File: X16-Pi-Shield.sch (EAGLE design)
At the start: 55 parts, among them J1 CONN_DF13-4P-1.25DSA, J2 CONN_DF13-4P-1.25DSA, J3 CONN_DF13-4P-1.25DSA, Q2 2.5A/30V/105mΩ, Q3 220mA/50V/3.5Ω, Q4 220mA/50V/3.5Ω, Q5 220mA/50V/3.5Ω, U2 MAX1136EUA-T, Y2 ECS-80-S-4X

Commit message: edited schematic for new connector
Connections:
- net GPIO_6 renamed SA0
- removed net N$42: U$1.3V3@1
- new net CTRL: U$1.GPIO22
- new net DGND: U$1.GPIO6
- new net SA1: U$1.GPIO18
- new net SALERT: U$1.GPIO13
- net 3V3: now also U$1.3V3@1
- net GPIO_10: no longer U$1.GPIO6
- net GPIO_11: no longer U$1.GPIO22
- net GPIO_7: no longer U$1.GPIO18
- net GPIO_8: no longer U$1.GPIO12
- net GPIO_9: no longer U$1.GPIO13
- net SCL: now also U$1.GPIO12
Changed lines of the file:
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@@
 <attribute name="SPICEPREFIX" value="X"/>
 </part>
+<part name="FRAME3" library="SparkFun-Aesthetics" library_urn="urn:adsk.eagle:library:507" deviceset="FRAME-A4L" device=""/>
 </parts>
 <sheets>
@@
 </segment>
 </net>
-<net name="GPIO_7" class="0">
-<segment>
-<pinref part="U$1" gate="G$1" pin="GPIO18"/>
-<wire x1="139.7" y1="160.02" x2="139.7" y2="167.64" width="0.1524" layer="91"/>
-<label x="139.7" y="162.56" size="1.778" layer="95" rot="R90"/>
-</segment>
-</net>
 <net name="GPIO_2" class="0">
 <segment>
@@
 </segment>
 </net>
-<net name="GPIO_8" class="0">
-<segment>
-<pinref part="U$1" gate="G$1" pin="GPIO12"/>
-<wire x1="190.5" y1="160.02" x2="190.5" y2="167.64" width="0.1524" layer="91"/>
-<label x="190.5" y="162.56" size="1.778" layer="95" rot="R90"/>
-</segment>
-</net>
 <net name="GPIO_1" class="0">
 <segment>
@@
 </segment>
 </net>
-<net name="GPIO_6" class="0">
-<segment>
-<pinref part="U$1" gate="G$1" pin="GPIO21"/>
-<wire x1="210.82" y1="160.02" x2="210.82" y2="167.64" width="0.1524" layer="91"/>
-<label x="210.82" y="162.56" size="1.778" layer="95" rot="R90"/>
-</segment>
-</net>
 <net name="INT" class="0">
 <segment>
@@
 </segment>
 </net>
-<net name="GPIO_9" class="0">
-<segment>
-<pinref part="U$1" gate="G$1" pin="GPIO13"/>
-<wire x1="195.58" y1="132.08" x2="195.58" y2="127" width="0.1524" layer="91"/>
-<label x="195.58" y="121.92" size="1.778" layer="95" rot="R90"/>
-</segment>
-</net>
-<net name="GPIO_10" class="0">
-<segment>
-<pinref part="U$1" gate="G$1" pin="GPIO6"/>
-<wire x1="190.5" y1="132.08" x2="190.5" y2="127" width="0.1524" layer="91"/>
-<label x="190.5" y="121.92" size="1.778" layer="95" rot="R90"/>
-</segment>
-</net>
 <net name="RX1_INT" class="0">
 <segment>
@@
 </segment>
 </net>
-<net name="GPIO_11" class="0">
-<segment>
-<pinref part="U$1" gate="G$1" pin="GPIO22"/>
-<wire x1="149.86" y1="132.08" x2="149.86" y2="127" width="0.1524" layer="91"/>
-<label x="149.86" y="121.92" size="1.778" layer="95" rot="R90"/>
-</segment>
-</net>
 <net name="IMU_INT" class="0">
 <segment>
@@
 <wire x1="142.24" y1="45.72" x2="134.62" y2="45.72" width="0.1524" layer="91"/>
 <label x="137.16" y="45.72" size="1.778" layer="95"/>
-</segment>
-</net>
-<net name="N$42" class="0">
-<segment>
-<pinref part="U$1" gate="G$1" pin="3V3@1"/>
-<wire x1="114.3" y1="132.08" x2="114.3" y2="129.54" width="0.1524" layer="91"/>
 </segment>
 </net>
@@
 <wire x1="83.82" y1="170.18" x2="73.66" y2="170.18" width="0.1524" layer="91"/>
 </segment>
+<segment>
+<pinref part="U$1" gate="G$1" pin="3V3@1"/>
+<wire x1="114.3" y1="132.08" x2="114.3" y2="129.54" width="0.1524" layer="91"/>
+<label x="114.3" y="127" size="1.778" layer="95" rot="R90"/>
+</segment>
 </net>
 <net name="SCL" class="0">
@@
 <wire x1="45.72" y1="101.6" x2="33.02" y2="101.6" width="0.1524" layer="91"/>
 <label x="35.56" y="101.6" size="1.778" layer="95"/>
+</segment>
+<segment>
+<pinref part="U$1" gate="G$1" pin="GPIO12"/>
+<wire x1="190.5" y1="160.02" x2="190.5" y2="167.64" width="0.1524" layer="91"/>
+<label x="190.5" y="162.56" size="1.778" layer="95" rot="R90"/>
 </segment>
 </net>
@@
 </segment>
 </net>
+<net name="CTRL" class="0">
+<segment>
+<pinref part="U$1" gate="G$1" pin="GPIO22"/>
+<wire x1="149.86" y1="132.08" x2="149.86" y2="127" width="0.1524" layer="91"/>
+<label x="149.86" y="127" size="1.778" layer="95" rot="R90"/>
+</segment>
+</net>
+<net name="DGND" class="0">
+<segment>
+<pinref part="U$1" gate="G$1" pin="GPIO6"/>
+<wire x1="190.5" y1="132.08" x2="190.5" y2="127" width="0.1524" layer="91"/>
+<label x="190.5" y="124.46" size="1.778" layer="95" rot="R90"/>
+</segment>
+</net>
+<net name="SALERT" class="0">
+<segment>
+<pinref part="U$1" gate="G$1" pin="GPIO13"/>
+<wire x1="195.58" y1="132.08" x2="195.58" y2="127" width="0.1524" layer="91"/>
+<label x="195.58" y="121.92" size="1.778" layer="95" rot="R90"/>
+</segment>
+</net>
+<net name="SA1" class="0">
+<segment>
+<pinref part="U$1" gate="G$1" pin="GPIO18"/>
+<wire x1="139.7" y1="160.02" x2="139.7" y2="167.64" width="0.1524" layer="91"/>
+<label x="139.7" y="162.56" size="1.778" layer="95" rot="R90"/>
+</segment>
+</net>
+<net name="SA0" class="0">
+<segment>
+<pinref part="U$1" gate="G$1" pin="GPIO21"/>
+<wire x1="210.82" y1="160.02" x2="210.82" y2="167.64" width="0.1524" layer="91"/>
+<label x="210.82" y="162.56" size="1.778" layer="95" rot="R90"/>
+</segment>
+</net>
 </nets>
 </sheet>
@@
 </nets>
 </sheet>
+<sheet>
+<plain>
+</plain>
+<instances>
+<instance part="FRAME3" gate="G$1" x="0" y="0" smashed="yes">
+<attribute name="DRAWING_NAME" x="181.61" y="11.43" size="2.54" layer="94" font="vector"/>
+<attribute name="LAST_DATE_TIME" x="181.61" y="6.35" size="2.286" layer="94" font="vector"/>
+<attribute name="SHEET" x="195.58" y="1.27" size="2.54" layer="94" font="vector"/>
+<attribute name="DESIGNER" x="226.26" y="6.35" size="2.54" layer="94" font="vector"/>
+</instance>
+</instances>
+<busses>
+</busses>
+<nets>
+</nets>
+</sheet>
 </sheets>
 </schematic>
@@
 which will not be processed correctly with this version.
 </note>
+<note version="8.2" severity="warning">
+Since Version 8.2, EAGLE supports online libraries. The ids
+of those online libraries will not be understood (or retained)
+with this version.
+</note>
+<note version="8.3" severity="warning">
+Since Version 8.3, EAGLE supports URNs for individual library
+assets (packages, symbols, and devices). The URNs of those assets
+will not be understood (or retained) with this version.
+</note>
 </compatibility>

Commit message: added connector
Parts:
- added J4: SAMTEC-HTST-110-04-X-D-RAJ, SAMTEC-HTST-110-04-X-D-RA:SAMTEC-HTST-110-04-X-D-RAJ
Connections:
- net 5V: now also J4.1
- net CLK: now also J4.18
- net CS: now also J4.20
- net CTRL: now also J4.7
- net DGND: now also J4.9
- net GND: now also J4.3
- net GPIO1: now also J4.2
- net GPIO2: now also J4.4
- net GPIO3: now also J4.6
- net GPIO4: now also J4.8
- net MISO: now also J4.14
- net MOSI: now also J4.16
- net SA0: now also J4.19
- net SA1: now also J4.17
- net SALERT: now also J4.13
- net SCL: now also J4.15
- net SDA: now also J4.11
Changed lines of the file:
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@@
 </part>
 <part name="FRAME3" library="SparkFun-Aesthetics" library_urn="urn:adsk.eagle:library:507" deviceset="FRAME-A4L" device=""/>
+<part name="J4" library="SAMTEC-HTST-110-04-X-D-RA" deviceset="SAMTEC-HTST-110-04-X-D-RA" device="J"/>
 </parts>
 <sheets>
@@
 <attribute name="DESIGNER" x="226.26" y="6.35" size="2.54" layer="94" font="vector"/>
 </instance>
+<instance part="J4" gate="A" x="50.8" y="102.87" smashed="yes">
+<attribute name="NAME" x="50.8" y="107.95" size="2.54" layer="95"/>
+<attribute name="VALUE" x="50.8" y="69.85" size="2.286" layer="96"/>
+</instance>
 </instances>
 <busses>
 </busses>
 <nets>
+<net name="GPIO1" class="0">
+<segment>
+<pinref part="J4" gate="A" pin="2"/>
+<wire x1="76.2" y1="102.87" x2="82.55" y2="102.87" width="0.1524" layer="91"/>
+<label x="82.55" y="102.87" size="1.778" layer="95"/>
+</segment>
+</net>
+<net name="GPIO2" class="0">
+<segment>
+<pinref part="J4" gate="A" pin="4"/>
+<wire x1="76.2" y1="100.33" x2="82.55" y2="100.33" width="0.1524" layer="91"/>
+<label x="82.55" y="100.33" size="1.778" layer="95"/>
+</segment>
+</net>
+<net name="GPIO3" class="0">
+<segment>
+<pinref part="J4" gate="A" pin="6"/>
+<wire x1="76.2" y1="97.79" x2="82.55" y2="97.79" width="0.1524" layer="91"/>
+<label x="82.55" y="97.79" size="1.778" layer="95"/>
+</segment>
+</net>
+<net name="GPIO4" class="0">
+<segment>
+<pinref part="J4" gate="A" pin="8"/>
+<wire x1="76.2" y1="95.25" x2="82.55" y2="95.25" width="0.1524" layer="91"/>
+<label x="82.55" y="95.25" size="1.778" layer="95"/>
+</segment>
+</net>
+<net name="5V" class="0">
+<segment>
+<pinref part="J4" gate="A" pin="1"/>
+<wire x1="45.72" y1="102.87" x2="39.37" y2="102.87" width="0.1524" layer="91"/>
+<label x="39.37" y="102.87" size="1.778" layer="95"/>
+</segment>
+</net>
+<net name="GND" class="0">
+<segment>
+<pinref part="J4" gate="A" pin="3"/>
+<wire x1="45.72" y1="100.33" x2="39.37" y2="100.33" width="0.1524" layer="91"/>
+<label x="39.37" y="100.33" size="1.778" layer="95"/>
+</segment>
+</net>
+<net name="MOSI" class="0">
+<segment>
+<pinref part="J4" gate="A" pin="16"/>
+<wire x1="76.2" y1="85.09" x2="82.55" y2="85.09" width="0.1524" layer="91"/>
+<label x="82.55" y="85.09" size="1.778" layer="95"/>
+</segment>
+</net>
+<net name="MISO" class="0">
+<segment>
+<pinref part="J4" gate="A" pin="14"/>
+<wire x1="76.2" y1="87.63" x2="82.55" y2="87.63" width="0.1524" layer="91"/>
+<label x="82.55" y="87.63" size="1.778" layer="95"/>
+</segment>
+</net>
+<net name="CTRL" class="0">
+<segment>
+<pinref part="J4" gate="A" pin="7"/>
+<wire x1="45.72" y1="95.25" x2="39.37" y2="95.25" width="0.1524" layer="91"/>
+<label x="39.37" y="95.25" size="1.778" layer="95" rot="R180"/>
+</segment>
+</net>
+<net name="DGND" class="0">
+<segment>
+<pinref part="J4" gate="A" pin="9"/>
+<wire x1="45.72" y1="92.71" x2="39.37" y2="92.71" width="0.1524" layer="91"/>
+<label x="39.37" y="92.71" size="1.778" layer="95" rot="R180"/>
+</segment>
+</net>
+<net name="SDA" class="0">
+<segment>
+<pinref part="J4" gate="A" pin="11"/>
+<wire x1="45.72" y1="90.17" x2="39.37" y2="90.17" width="0.1524" layer="91"/>
+<label x="39.37" y="90.17" size="1.778" layer="95" rot="R180"/>
+</segment>
+</net>
+<net name="SALERT" class="0">
+<segment>
+<pinref part="J4" gate="A" pin="13"/>
+<wire x1="45.72" y1="87.63" x2="39.37" y2="87.63" width="0.1524" layer="91"/>
+<label x="39.37" y="87.63" size="1.778" layer="95" rot="R180"/>
+</segment>
+</net>
+<net name="SCL" class="0">
+<segment>
+<pinref part="J4" gate="A" pin="15"/>
+<wire x1="45.72" y1="85.09" x2="39.37" y2="85.09" width="0.1524" layer="91"/>
+<label x="39.37" y="85.09" size="1.778" layer="95" rot="R180"/>
+</segment>
+</net>
+<net name="SA1" class="0">
+<segment>
+<pinref part="J4" gate="A" pin="17"/>
+<wire x1="45.72" y1="82.55" x2="39.37" y2="82.55" width="0.1524" layer="91"/>
+<label x="39.37" y="82.55" size="1.778" layer="95" rot="R180"/>
+</segment>
+</net>
+<net name="SA0" class="0">
+<segment>
+<pinref part="J4" gate="A" pin="19"/>
+<wire x1="45.72" y1="80.01" x2="39.37" y2="80.01" width="0.1524" layer="91"/>
+<label x="39.37" y="80.01" size="1.778" layer="95" rot="R180"/>
+</segment>
+</net>
+<net name="CS" class="0">
+<segment>
+<pinref part="J4" gate="A" pin="20"/>
+<wire x1="76.2" y1="80.01" x2="82.55" y2="80.01" width="0.1524" layer="91"/>
+<label x="82.55" y="80.01" size="1.778" layer="95"/>
+</segment>
+</net>
+<net name="CLK" class="0">
+<segment>
+<pinref part="J4" gate="A" pin="18"/>
+<wire x1="76.2" y1="82.55" x2="81.28" y2="82.55" width="0.1524" layer="91"/>
+<wire x1="81.28" y1="82.55" x2="81.28" y2="83.82" width="0.1524" layer="91"/>
+<label x="81.28" y="81.28" size="1.778" layer="95"/>
+</segment>
+</net>
 </nets>
 </sheet>

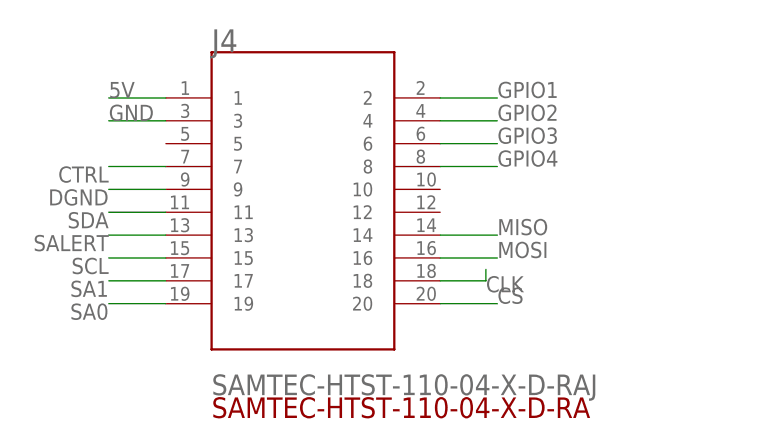
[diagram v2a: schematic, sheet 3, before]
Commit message: added some nets
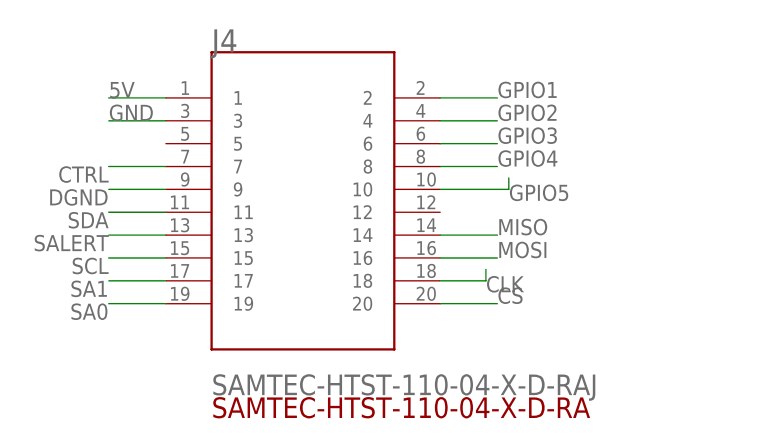
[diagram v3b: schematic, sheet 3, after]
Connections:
- removed net N$34: U$1.3V3@17
- net 3V3: now also U$1.3V3@17
- net GPIO5: now also J4.10
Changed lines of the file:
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@@
-</segment>
-</net>
-<net name="N$34" class="0">
-<segment>
-<pinref part="U$1" gate="G$1" pin="3V3@17"/>
-<wire x1="154.94" y1="132.08" x2="154.94" y2="127" width="0.1524" layer="91"/>
 </segment>
 </net>
@@
 <wire x1="114.3" y1="132.08" x2="114.3" y2="129.54" width="0.1524" layer="91"/>
 <label x="114.3" y="127" size="1.778" layer="95" rot="R90"/>
+</segment>
+<segment>
+<pinref part="U$1" gate="G$1" pin="3V3@17"/>
+<wire x1="154.94" y1="132.08" x2="154.94" y2="127" width="0.1524" layer="91"/>
+<label x="154.94" y="127" size="1.778" layer="95" rot="R90"/>
 </segment>
 </net>
@@
 </segment>
 </net>
+<net name="GPIO5" class="0">
+<segment>
+<pinref part="J4" gate="A" pin="10"/>
+<wire x1="76.2" y1="92.71" x2="83.82" y2="92.71" width="0.1524" layer="91"/>
+<wire x1="83.82" y1="92.71" x2="83.82" y2="93.98" width="0.1524" layer="91"/>
+<label x="83.82" y="91.44" size="1.778" layer="95"/>
+</segment>
+</net>

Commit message: fixed library problems
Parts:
- removed C7: 4.7uF, SparkFun-Capacitors:4.7UF0603
- removed JP5: JUMPER-SMT_2_NO_SILK, SparkFun-Jumpers:JUMPER-SMT_2_NO_SILK
- removed U$3: ADAFRUIT-FXOS8700-FXAS21002, X15-Pi-Shield-Parts:ADAFRUIT-FXOS8700-FXAS21002
- removed U$5: ADAFRUIT-BNO055, X15-Pi-Shield-Parts:ADAFRUIT-BNO055
- removed U$9: 8X_CONN, X15-Pi-Shield-Parts:8X_CONN
- added C3: 4.7uF, SparkFun-Capacitors:4.7UF0603
- added JP7: JUMPER-SMT_2_NO_SILK, SparkFun-Jumpers:JUMPER-SMT_2_NO_SILK
- added U$2: CONN_ADAFRUIT-BNO055, X16-Pi-Shield:CONN_ADAFRUIT-BNO055
- added U$4: CONN_ADAFRUIT-FXOS8700-FXAS21002, X16-Pi-Shield:CONN_ADAFRUIT-FXOS8700-FXAS21002
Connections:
- removed net 3VO_2: U$5.3VO
- removed net A_INT1: U$3.AI1
- removed net GPIO6: U$9.24
- removed net GPIO_10: U$9.2
- removed net GPIO_11: U$9.15
- removed net GPIO_7: U$9.1
- removed net GPIO_8: U$9.4
- removed net GPIO_9: U$9.3
- removed net IMU_INT1: U$3.GI1
- removed net IMU_RESET1: U$3.RST
- removed net N$8: JP5.2, U$5.ADR
- removed net SCL1: U$3.SCL
- removed net SDA1: U$3.SDA
- new net 3V0_2: U$2.3VO
- new net N$17: JP7.2, U$2.ADR
- net 3V3: now also C3.1, JP7.1, U$2.VIN, U$4.VIN; no longer C7.1, JP5.1, U$3.VIN, U$5.VIN, U$9.23
- net 3VO_1: now also U$4.3VO; no longer U$3.3VO
- net 5V: no longer U$9.19
- net A_INT: now also U$4.AI1
- net GND: now also C3.2, U$2.GND, U$4.GND; no longer C7.2, U$3.GND, U$5.GND, U$9.17, U$9.21
- net GPIO1: no longer U$9.14
- net GPIO2: no longer U$9.16
- net GPIO3: no longer U$9.18
- net GPIO4: no longer U$9.20
- net GPIO5: no longer U$9.22
- net IMU_INT: now also U$2.INT, U$4.GI1; no longer U$5.INT
- net IMU_RESET: now also U$2.RST, U$4.RST; no longer U$5.RST
- net SCL: now also U$2.SCL, U$4.SCL; no longer U$5.SCL
- net SDA: now also U$2.SDA, U$4.SDA; no longer U$5.SDA

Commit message: made some changes
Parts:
- U$7: device X15-Pi-Shield-Parts:DISCRETECOMPONENTS_SWITCH -> X16-Pi-Shield:SWITCH_DISCRETECOMPONENTS
- U$8: value MCR1101 -> IC_MCR1101; device X15-Pi-Shield-Parts:MCR1101 -> X16-Pi-Shield:IC_MCR1101
- U2: device X15-Pi-Shield-Parts:MAX1136EUA-T -> X16-Pi-Shield:MAX1136EUA-T
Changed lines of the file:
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@@
 <part name="GND43" library="SparkFun-PowerSymbols" deviceset="GND" device=""/>
 <part name="GND44" library="SparkFun-PowerSymbols" deviceset="GND" device=""/>
-<part name="U$8" library="X15-Pi-Shield-Parts" deviceset="MCR1101" device=""/>
+<part name="U$8" library="X16-Pi-Shield" deviceset="IC_MCR1101" device=""/>
 <part name="C10" library="SparkFun-Capacitors" deviceset="0.1UF" device="-0603-25V-(+80/-20%)" value="0.1uF"/>
 <part name="C11" library="SparkFun-Capacitors" deviceset="10NF" device="-0603-50V-10%" value="10nF"/>
@@
 <part name="R22" library="SparkFun-Resistors" deviceset="RESISTOR" device="0603" value="10k"/>
 <part name="Q3" library="SparkFun-DiscreteSemi" deviceset="MOSFET-NCH" device="-BSS138" value="220mA/50V/3.5Ω"/>
-<part name="U$7" library="X15-Pi-Shield-Parts" deviceset="DISCRETECOMPONENTS_SWITCH" device=""/>
+<part name="U$7" library="X16-Pi-Shield" deviceset="SWITCH_DISCRETECOMPONENTS" device="" package3d_urn="urn:adsk.eagle:package:24384574/2"/>
 <part name="GND39" library="SparkFun-PowerSymbols" deviceset="GND" device=""/>
 <part name="GND40" library="SparkFun-PowerSymbols" deviceset="GND" device=""/>
@@
 <part name="GND31" library="SparkFun-PowerSymbols" deviceset="GND" device=""/>
 <part name="GND32" library="SparkFun-PowerSymbols" deviceset="GND" device=""/>
-<part name="U2" library="X15-Pi-Shield-Parts" deviceset="MAX1136EUA-T" device=""/>
+<part name="U2" library="X16-Pi-Shield" deviceset="MAX1136EUA-T" device=""/>
 <part name="GND34" library="SparkFun-PowerSymbols" deviceset="GND" device=""/>
 <part name="GND35" library="SparkFun-PowerSymbols" deviceset="GND" device=""/>
@@
 will not be understood (or retained) with this version.
 </note>
+<note version="8.3" severity="warning">
+Since Version 8.3, EAGLE supports the association of 3D packages
+with devices in libraries, schematics, and board files. Those 3D
+packages will not be understood (or retained) with this version.
+</note>
 </compatibility>

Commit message: updated schematic and library
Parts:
- removed C10, C12, C13: 0.1uF, SparkFun-Capacitors:0.1UF-0603-25V-(+80/-20%)
- removed C11: 10nF, SparkFun-Capacitors:10NF-0603-50V-10%
- removed Q4, Q5: 220mA/50V/3.5Ω, SparkFun-DiscreteSemi:MOSFET-NCH-BSS138
- removed R23, R24, R25, R26: 10k, SparkFun-Resistors:RESISTOR0603
- removed U$8: IC_MCR1101, X16-Pi-Shield:IC_MCR1101
- added C4: 10uF, SparkFun-Capacitors:2.2UF-0603-10V-20%
- added C5: 22uF, SparkFun-Capacitors:2.2UF-0603-10V-20%
- added U1: INA260AIPW, X16-Pi-Shield:INA260AIPW
- U2: value MAX1136EUA-T -> AZ1117IH-3.3TRG1; device X16-Pi-Shield:MAX1136EUA-T -> X16-Pi-Shield:AZ1117IH-3.3TRG1
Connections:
- removed net AMP_OUT: U$8.VOUT, U2.AIN1
- removed net GPIO5: J4.10
- removed net GPIO_5: U$1.GPIO20
- removed net N$11: C11.1, U$8.VCAP
- removed net POWER: U$1.5V@2, U$1.5V@4
- removed net SCL_ADC: Q4.D, R23.1, U2.SCL
- removed net SDA_ADC: Q5.D, R26.1, U2.SDA
- new net 5V_EXT: C4.2, J4.1, U1.IN+, U1.VBUS, U2.INPUT
- new net ALERT: U$1.GPIO20, U1.ALERT
- new net VS: C5.2, U1.VS, U2.OUTPUT
- net !AMP_FAULT: no longer U$8.!FAULTB
- net 3V3: no longer Q4.G, Q5.G, R24.1, R25.1
- net 5V: now also U$1.5V@2, U$1.5V@4, U1.IN-; no longer C10.1, C12.1, C13.1, J4.1, R23.2, R26.2, U$8.IP-, U$8.VCC, U2.AIN3/REF, U2.VDD
- net 5V_RAW: no longer U$8.IP+
- net AIN2: no longer U2.AIN2
- net GND: now also C4.1, C5.1, U1.GND; no longer C10.2, C11.2, C12.2, C13.2, U$8.GND
- net OCD: no longer U$8.VOC
- net SA0: now also U1.AO
- net SA1: now also U1.A1
- net SCL: now also U1.SCL; no longer Q4.S, R24.2
- net SDA: now also U1.SDA; no longer Q5.S, R25.2
